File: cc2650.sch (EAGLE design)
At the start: 21 parts, among them IC4 CC2650MODAMOHR, SW1 SPST_TACT-KMR2, SW2 SPST_TACT-KMR2, U402 TPS62233DRY

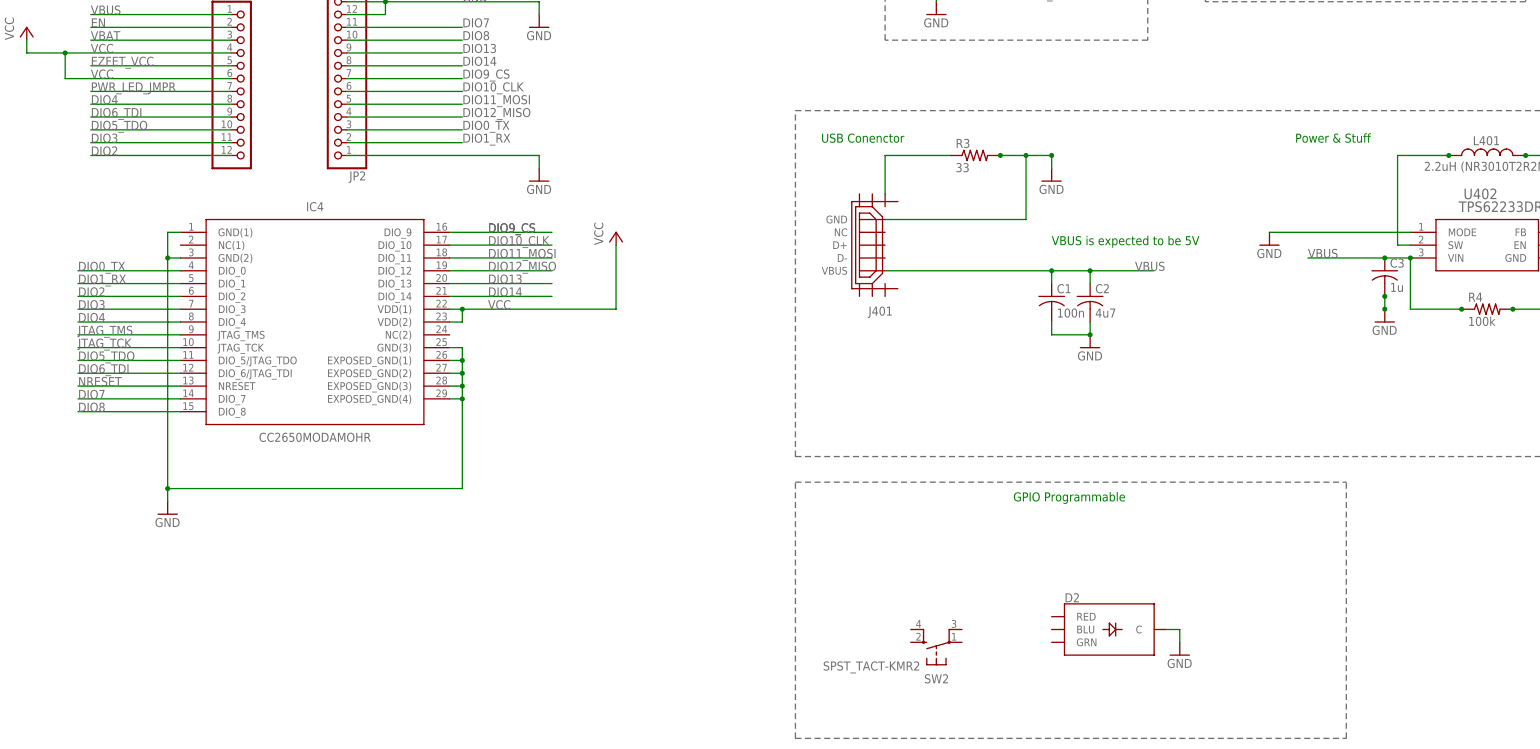
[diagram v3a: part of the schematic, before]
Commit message: added connections for RGB LED and push button.
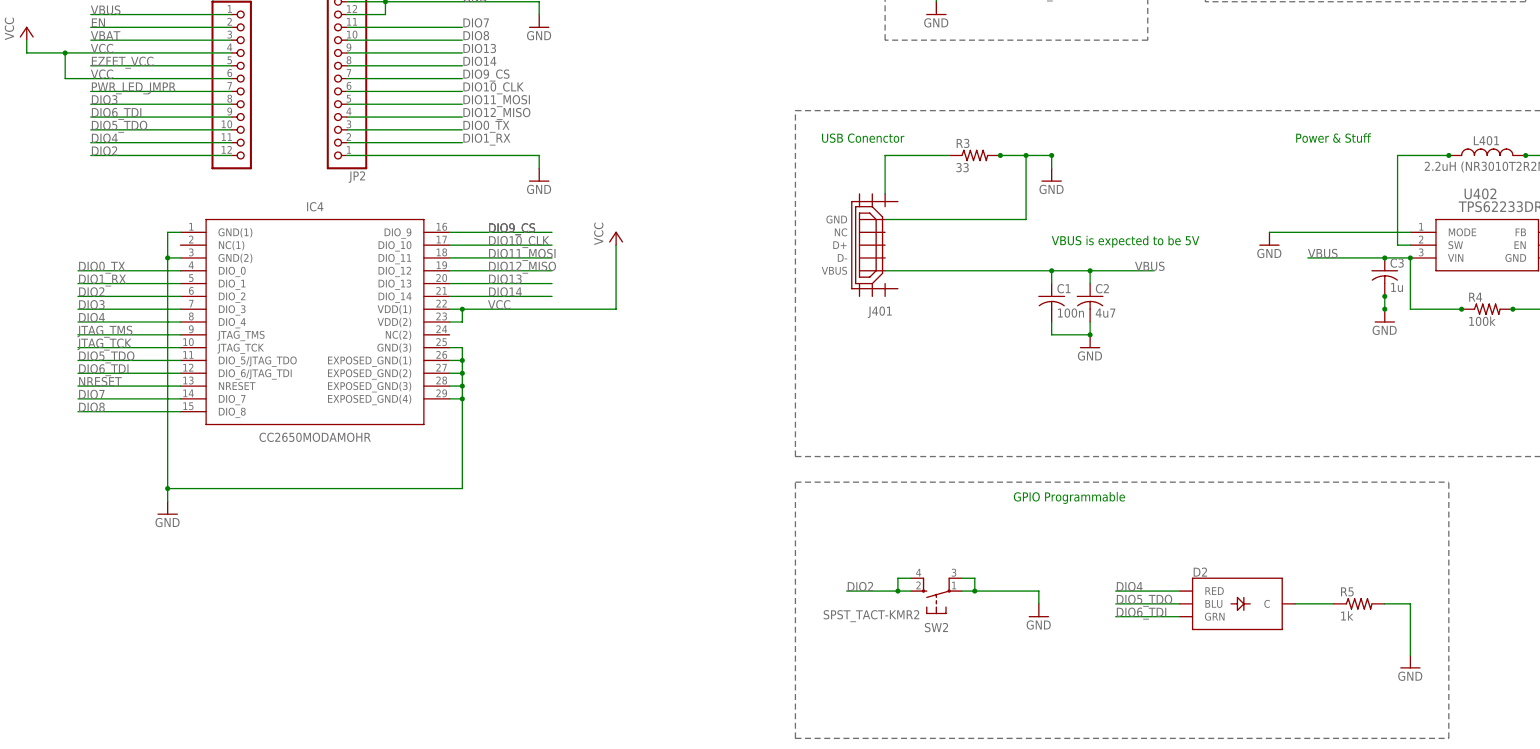
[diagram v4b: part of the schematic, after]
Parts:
- added R5: 1k, adafruit:R-US_R0402
- R4: MF VISHAY/DALE -> (none); MPN CRCW0805100KFKTA -> RC0603JR-07100KL; OC_NEWARK 05F1513 -> 68R0147
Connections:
- new net N$2: D2.C, R5.1
- net DIO2: now also SW2.S, SW2.S1
- net DIO3: now also JP3.8; no longer JP3.11
- net DIO4: now also D2.RED, JP3.11; no longer JP3.8
- net DIO5_TDO: now also D2.BLU
- net DIO6_TDI: now also D2.GRN
- net GND: now also R5.2, SW2.P, SW2.P1; no longer D2.C
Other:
- moved on the sheet: D2, SW2
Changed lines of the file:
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@@
 </part>
 <part name="R4" library="adafruit" deviceset="R-US_" device="R0603" value="100k">
-<attribute name="MF" value="VISHAY/DALE"/>
-<attribute name="MPN" value="CRCW0805100KFKTA"/>
-<attribute name="OC_NEWARK" value="05F1513"/>
+<attribute name="MF" value=""/>
+<attribute name="MPN" value="RC0603JR-07100KL"/>
+<attribute name="OC_NEWARK" value="68R0147"/>
 </part>
 <part name="P+2" library="supply1" library_urn="urn:adsk.eagle:library:371" deviceset="VCC" device=""/>
@@
 </part>
 <part name="GND6" library="supply1" library_urn="urn:adsk.eagle:library:371" deviceset="GND" device=""/>
+<part name="GND8" library="supply1" library_urn="urn:adsk.eagle:library:371" deviceset="GND" device=""/>
+<part name="R5" library="adafruit" deviceset="R-US_" device="R0402" value="1k">
+<attribute name="MF" value=""/>
+<attribute name="MPN" value="ERA-2AEB471X"/>
+<attribute name="OC_NEWARK" value="08N2086"/>
+</part>
 </parts>
 <sheets>
@@
 <wire x1="17.78" y1="-36.83" x2="240.03" y2="-36.83" width="0.1524" layer="95" style="shortdash"/>
 <wire x1="17.78" y1="-92.71" x2="17.78" y2="-41.91" width="0.1524" layer="95" style="shortdash"/>
-<wire x1="17.78" y1="-41.91" x2="127" y2="-41.91" width="0.1524" layer="95" style="shortdash"/>
-<wire x1="127" y1="-92.71" x2="127" y2="-41.91" width="0.1524" layer="95" style="shortdash"/>
-<wire x1="17.78" y1="-92.71" x2="127" y2="-92.71" width="0.1524" layer="95" style="shortdash"/>
+<wire x1="17.78" y1="-41.91" x2="147.32" y2="-41.91" width="0.1524" layer="95" style="shortdash"/>
+<wire x1="147.32" y1="-92.71" x2="147.32" y2="-41.91" width="0.1524" layer="95" style="shortdash"/>
+<wire x1="17.78" y1="-92.71" x2="147.32" y2="-92.71" width="0.1524" layer="95" style="shortdash"/>
 <text x="60.96" y="-45.72" size="1.778" layer="91">GPIO Programmable</text>
 <text x="-142.24" y="71.12" size="1.778" layer="91">Add jumper from 3 &amp; 4 to use battery.
@@
 <attribute name="MPN" x="55.88" y="60.96" size="1.778" layer="96" display="off"/>
 </instance>
-<instance part="SW2" gate="G$1" x="45.72" y="-73.66" rot="R90">
-<attribute name="OC_NEWARK" x="45.72" y="-73.66" size="1.778" layer="96" display="off"/>
-<attribute name="MF" x="45.72" y="-73.66" size="1.778" layer="96" display="off"/>
-<attribute name="MPN" x="45.72" y="-73.66" size="1.778" layer="96" display="off"/>
+<instance part="SW2" gate="G$1" x="45.72" y="-63.5" rot="R90">
+<attribute name="OC_NEWARK" x="45.72" y="-63.5" size="1.778" layer="96" display="off"/>
+<attribute name="MF" x="45.72" y="-63.5" size="1.778" layer="96" display="off"/>
+<attribute name="MPN" x="45.72" y="-63.5" size="1.778" layer="96" display="off"/>
 </instance>
 <instance part="GND3" gate="1" x="-33.02" y="48.26"/>
@@
 </instance>
 <instance part="GND4" gate="1" x="228.6" y="-25.4"/>
-<instance part="GND5" gate="1" x="93.98" y="-76.2"/>
-<instance part="D2" gate="G$1" x="78.74" y="-71.12">
-<attribute name="OC_NEWARK" x="78.74" y="-71.12" size="1.778" layer="96" display="off"/>
-<attribute name="MF" x="78.74" y="-71.12" size="1.778" layer="96" display="off"/>
-<attribute name="MPN" x="78.74" y="-71.12" size="1.778" layer="96" display="off"/>
+<instance part="GND5" gate="1" x="139.7" y="-78.74"/>
+<instance part="D2" gate="G$1" x="104.14" y="-66.04">
+<attribute name="OC_NEWARK" x="104.14" y="-66.04" size="1.778" layer="96" display="off"/>
+<attribute name="MF" x="104.14" y="-66.04" size="1.778" layer="96" display="off"/>
+<attribute name="MPN" x="104.14" y="-66.04" size="1.778" layer="96" display="off"/>
 </instance>
 <instance part="JP3" gate="G$1" x="-91.44" y="35.56">
@@
 </instance>
 <instance part="GND6" gate="1" x="-33.02" y="17.78"/>
+<instance part="GND8" gate="1" x="66.04" y="-68.58"/>
+<instance part="R5" gate="G$1" x="129.54" y="-66.04">
+<attribute name="OC_NEWARK" x="129.54" y="-66.04" size="1.778" layer="96" display="off"/>
+<attribute name="MF" x="129.54" y="-66.04" size="1.778" layer="96" display="off"/>
+<attribute name="MPN" x="129.54" y="-66.04" size="1.778" layer="96" display="off"/>
+</instance>
 </instances>
 <busses>
@@
 </segment>
 <segment>
-<pinref part="D2" gate="G$1" pin="C"/>
-<wire x1="91.44" y1="-71.12" x2="93.98" y2="-71.12" width="0.1524" layer="91"/>
 <pinref part="GND5" gate="1" pin="GND"/>
-<wire x1="93.98" y1="-71.12" x2="93.98" y2="-73.66" width="0.1524" layer="91"/>
+<wire x1="139.7" y1="-66.04" x2="139.7" y2="-76.2" width="0.1524" layer="91"/>
+<pinref part="R5" gate="G$1" pin="2"/>
+<wire x1="134.62" y1="-66.04" x2="139.7" y2="-66.04" width="0.1524" layer="91"/>
 </segment>
 <segment>
@@
 <pinref part="JP2" gate="A" pin="1"/>
 <wire x1="-71.12" y1="22.86" x2="-33.02" y2="22.86" width="0.1524" layer="91"/>
+</segment>
+<segment>
+<pinref part="GND8" gate="1" pin="GND"/>
+<wire x1="66.04" y1="-66.04" x2="66.04" y2="-63.5" width="0.1524" layer="91"/>
+<pinref part="SW2" gate="G$1" pin="P"/>
+<wire x1="66.04" y1="-63.5" x2="53.34" y2="-63.5" width="0.1524" layer="91"/>
+<pinref part="SW2" gate="G$1" pin="P1"/>
+<wire x1="53.34" y1="-63.5" x2="50.8" y2="-63.5" width="0.1524" layer="91"/>
+<wire x1="50.8" y1="-60.96" x2="53.34" y2="-60.96" width="0.1524" layer="91"/>
+<wire x1="53.34" y1="-60.96" x2="53.34" y2="-63.5" width="0.1524" layer="91"/>
+<junction x="53.34" y="-63.5"/>
 </segment>
 </net>
@@
 <label x="-121.92" y="27.94" size="1.778" layer="95"/>
 </segment>
+<segment>
+<pinref part="D2" gate="G$1" pin="BLU"/>
+<wire x1="93.98" y1="-66.04" x2="81.28" y2="-66.04" width="0.1524" layer="91"/>
+<label x="81.28" y="-66.04" size="1.778" layer="95"/>
+</segment>
 </net>
 <net name="DIO6_TDI" class="0">
@@
 <label x="-121.92" y="30.48" size="1.778" layer="95"/>
 </segment>
+<segment>
+<pinref part="D2" gate="G$1" pin="GRN"/>
+<wire x1="93.98" y1="-68.58" x2="81.28" y2="-68.58" width="0.1524" layer="91"/>
+<label x="81.28" y="-68.58" size="1.778" layer="95"/>
+</segment>
 </net>
 <net name="DIO7" class="0">
@@
 <label x="-121.92" y="22.86" size="1.778" layer="95"/>
 </segment>
+<segment>
+<pinref part="SW2" gate="G$1" pin="S"/>
+<wire x1="40.64" y1="-63.5" x2="38.1" y2="-63.5" width="0.1524" layer="91"/>
+<pinref part="SW2" gate="G$1" pin="S1"/>
+<wire x1="38.1" y1="-63.5" x2="27.94" y2="-63.5" width="0.1524" layer="91"/>
+<wire x1="40.64" y1="-60.96" x2="38.1" y2="-60.96" width="0.1524" layer="91"/>
+<wire x1="38.1" y1="-60.96" x2="38.1" y2="-63.5" width="0.1524" layer="91"/>
+<junction x="38.1" y="-63.5"/>
+<label x="27.94" y="-63.5" size="1.778" layer="95"/>
+</segment>
 </net>
 <net name="DIO3" class="0">
@@
 <segment>
 <label x="-124.46" y="-7.62" size="1.778" layer="95"/>
+</segment>
+<segment>
+<pinref part="JP3" gate="G$1" pin="8"/>
+<wire x1="-93.98" y1="33.02" x2="-121.92" y2="33.02" width="0.1524" layer="91"/>
+<label x="-121.92" y="33.02" size="1.778" layer="95"/>
+</segment>
+</net>
+<net name="DIO10_CLK" class="0">
+<segment>
+<pinref part="IC4" gate="G$1" pin="DIO_10"/>
+<wire x1="-50.8" y1="5.08" x2="-30.48" y2="5.08" width="0.1524" layer="91"/>
+<label x="-43.18" y="5.08" size="1.778" layer="95"/>
+</segment>
+<segment>
+<pinref part="JP2" gate="A" pin="6"/>
+<wire x1="-71.12" y1="35.56" x2="-48.26" y2="35.56" width="0.1524" layer="91"/>
+<label x="-48.26" y="35.56" size="1.778" layer="95"/>
+</segment>
+</net>
+<net name="DIO4" class="0">
+<segment>
+<pinref part="IC4" gate="G$1" pin="DIO_4"/>
+<wire x1="-104.14" y1="-10.16" x2="-124.46" y2="-10.16" width="0.1524" layer="91"/>
+</segment>
+<segment>
+<label x="-124.46" y="-10.16" size="1.778" layer="95"/>
 </segment>
 <segment>
@@
 <label x="-121.92" y="25.4" size="1.778" layer="95"/>
 </segment>
-</net>
-<net name="DIO10_CLK" class="0">
-<segment>
-<pinref part="IC4" gate="G$1" pin="DIO_10"/>
-<wire x1="-50.8" y1="5.08" x2="-30.48" y2="5.08" width="0.1524" layer="91"/>
-<label x="-43.18" y="5.08" size="1.778" layer="95"/>
-</segment>
-<segment>
-<pinref part="JP2" gate="A" pin="6"/>
-<wire x1="-71.12" y1="35.56" x2="-48.26" y2="35.56" width="0.1524" layer="91"/>
-<label x="-48.26" y="35.56" size="1.778" layer="95"/>
-</segment>
-</net>
-<net name="DIO4" class="0">
-<segment>
-<pinref part="IC4" gate="G$1" pin="DIO_4"/>
-<wire x1="-104.14" y1="-10.16" x2="-124.46" y2="-10.16" width="0.1524" layer="91"/>
-</segment>
-<segment>
-<label x="-124.46" y="-10.16" size="1.778" layer="95"/>
-</segment>
-<segment>
-<pinref part="JP3" gate="G$1" pin="8"/>
-<wire x1="-93.98" y1="33.02" x2="-121.92" y2="33.02" width="0.1524" layer="91"/>
-<label x="-121.92" y="33.02" size="1.778" layer="95"/>
+<segment>
+<pinref part="D2" gate="G$1" pin="RED"/>
+<wire x1="93.98" y1="-63.5" x2="81.28" y2="-63.5" width="0.1524" layer="91"/>
+<label x="81.28" y="-63.5" size="1.778" layer="95"/>
 </segment>
 </net>
@@
 </segment>
 </net>
+<net name="N$2" class="0">
+<segment>
+<pinref part="D2" gate="G$1" pin="C"/>
+<pinref part="R5" gate="G$1" pin="1"/>
+<wire x1="116.84" y1="-66.04" x2="124.46" y2="-66.04" width="0.1524" layer="91"/>
+</segment>
+</net>

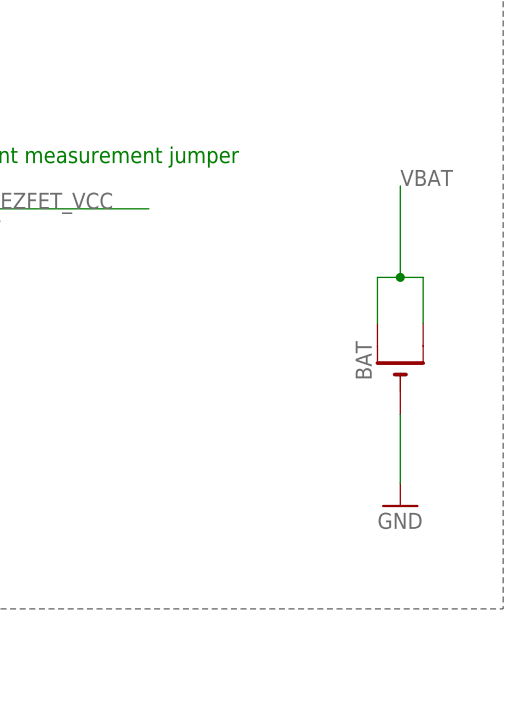
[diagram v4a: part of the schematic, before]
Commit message: Removed battery, ripped up connections to move things around and add sensors. Need to replace usb with through hole connector.
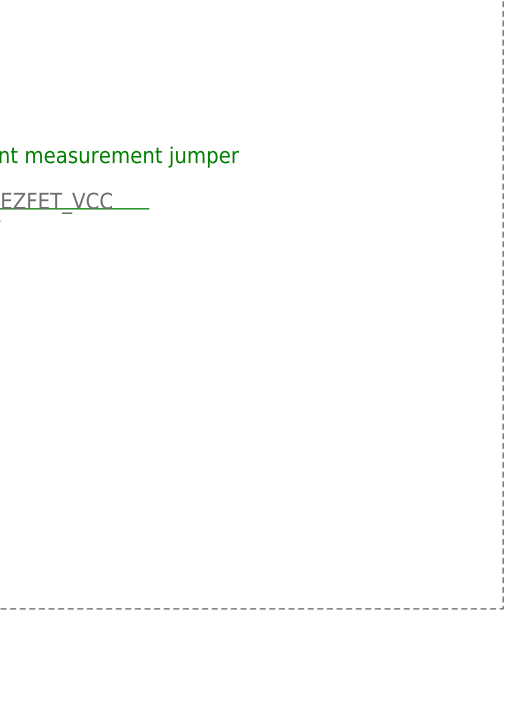
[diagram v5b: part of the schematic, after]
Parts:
- removed BAT: (no value), adafruit:CR1220THM
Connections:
- net GND: no longer BAT.-
- net VBAT: no longer BAT.+, BAT.+1
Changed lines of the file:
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@@
 <attribute name="OC_NEWARK" value="87K4752"/>
 </part>
-<part name="GND4" library="supply1" deviceset="GND" device=""/>
 <part name="GND5" library="supply1" library_urn="urn:adsk.eagle:library:371" deviceset="GND" device=""/>
 <part name="D2" library="SparkFun-LED" deviceset="LED-RGB-CC" device="PIRANHA">
@@
 <attribute name="MPN" value=""/>
 <attribute name="OC_NEWARK" value="unknown"/>
-</part>
-<part name="BAT" library="adafruit" deviceset="CR1220" device="THM">
-<attribute name="MF" value="KEYSTONE ELECTR"/>
-<attribute name="MPN" value="3000"/>
-<attribute name="OC_NEWARK" value="66F5622"/>
 </part>
 <part name="P+1" library="supply1" library_urn="urn:adsk.eagle:library:371" deviceset="VCC" device=""/>
@@
 <attribute name="MPN" x="154.94" y="22.86" size="1.778" layer="96" display="off"/>
 </instance>
-<instance part="GND4" gate="1" x="228.6" y="-25.4"/>
 <instance part="GND5" gate="1" x="139.7" y="-78.74"/>
 <instance part="D2" gate="G$1" x="104.14" y="-66.04">
@@
 <attribute name="MF" x="-73.66" y="40.64" size="1.778" layer="96" display="off"/>
 <attribute name="MPN" x="-73.66" y="40.64" size="1.778" layer="96" display="off"/>
-</instance>
-<instance part="BAT" gate="G$1" x="228.6" y="-10.16" rot="R90">
-<attribute name="OC_NEWARK" x="228.6" y="-10.16" size="1.778" layer="96" display="off"/>
-<attribute name="MF" x="228.6" y="-10.16" size="1.778" layer="96" display="off"/>
-<attribute name="MPN" x="228.6" y="-10.16" size="1.778" layer="96" display="off"/>
 </instance>
 <instance part="P+1" gate="VCC" x="-33.02" y="68.58"/>
@@
 </segment>
 <segment>
-<pinref part="GND4" gate="1" pin="GND"/>
-<pinref part="BAT" gate="G$1" pin="-"/>
-<wire x1="228.6" y1="-22.86" x2="228.6" y2="-15.24" width="0.1524" layer="91"/>
-</segment>
-<segment>
 <pinref part="GND6" gate="1" pin="GND"/>
 <wire x1="-33.02" y1="20.32" x2="-33.02" y2="22.86" width="0.1524" layer="91"/>
@@
 <net name="VBAT" class="0">
 <segment>
-<pinref part="BAT" gate="G$1" pin="+"/>
-<wire x1="226.06" y1="-5.08" x2="226.06" y2="0" width="0.1524" layer="91"/>
-<pinref part="BAT" gate="G$1" pin="+1"/>
-<wire x1="226.06" y1="0" x2="228.6" y2="0" width="0.1524" layer="91"/>
-<wire x1="228.6" y1="0" x2="231.14" y2="0" width="0.1524" layer="91"/>
-<wire x1="231.14" y1="0" x2="231.14" y2="-5.08" width="0.1524" layer="91"/>
-<wire x1="228.6" y1="0" x2="228.6" y2="10.16" width="0.1524" layer="91"/>
-<junction x="228.6" y="0"/>
-<label x="228.6" y="10.16" size="1.778" layer="95"/>
-</segment>
-<segment>
 <pinref part="JP3" gate="G$1" pin="3"/>

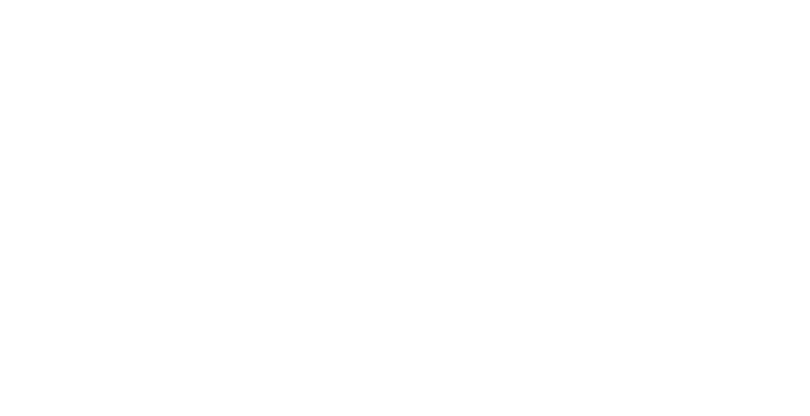
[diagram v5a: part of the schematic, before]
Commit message: Added light sensor.
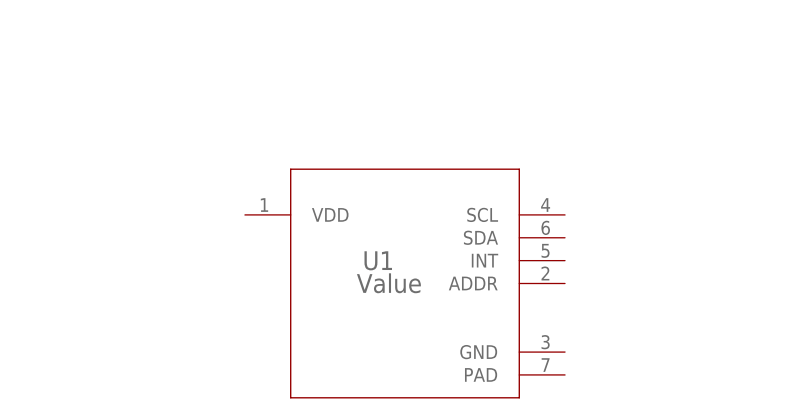
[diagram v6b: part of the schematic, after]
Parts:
- added U1: Value, OPT3001:OPT3001DNPR
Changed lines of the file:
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@@
 <attribute name="OC_NEWARK" value="08N2086"/>
 </part>
+<part name="U1" library="OPT3001" deviceset="OPT3001DNPR" device="" value="Value"/>
 </parts>
 <sheets>
@@
 <attribute name="MPN" x="129.54" y="-66.04" size="1.778" layer="96" display="off"/>
 </instance>
+<instance part="U1" gate="A" x="-76.2" y="-88.9"/>
 </instances>
 <busses>
